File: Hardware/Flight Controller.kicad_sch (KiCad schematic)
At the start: 93 parts, among them J1 9V / 12V, J2 USB4110GFA, U1 TPS54302, U2 STM32F722RETx, U3 AP2112K-3.3, U4 TPS54302, U5 ICM-42688-P, U6 BMP388, U7 USBLC6-2SC6, U8 AT7456E, U9 INA226, Y1 27Mhz, Y2 8MHz

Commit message: this commit updates MCU shematics, Flash memory and Magnetometer
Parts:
- added C47, C49: 0.1uF, Capacitor_SMD:C_0603_1608Metric, symbol Device:C_Small
- added C48: 4.7uF, Capacitor_SMD:C_0603_1608Metric, symbol Device:C_Small
- added R27, R28: 4.7k, Resistor_SMD:R_0402_1005Metric, symbol Device:R_Small
- added R29, R30, R31: 10k, Resistor_SMD:R_0402_1005Metric, symbol Device:R_Small
- added U10: QMC5883P, easyeda2kicad:LGA-16_L3.0-W3.0-P0.50-BL_SQ, symbol Magneto:QMC5883P
- added U11: W25Q128JVSIQ, W25Q128JVSIQ:SOIC127P790X216-8N, symbol flash:W25Q128JVSIQ
- C25, C26: value 0.1uF -> 30pF
- C44: value 1uF -> 10nF
- C45, C46: value 0.1uF -> 14pF
- Y1: value 27Mhz -> 27Mhz 20pF
- Y2: value 8MHz -> 8MHz 12pF
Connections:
- net BARO_SCL is gone; now on net BMP_SCL: U2.28 (PB10)
- net +3.3V: now also C49.1, R27.1, R28.1, R29.2, R30.1, R31.2, U11.8 (VCC)
- net ADC_Voltage: now also U2.25 (PB0); no longer U2.61 (PB8)
- net BMP_SCL: no longer R11.2, U6.4 (SDI)
- net GND: now also U2.12 (VSSA), U2.18 (VSS), U2.31 (VSS), U2.47 (VSS), U2.63 (VSS), C47.2, C48.2, C49.2, U11.4 (GND)
- net OSD_CS: now also U2.33 (PB12)
- net OSD_MISO: now also U2.10 (PC2)
- net OSD_MOSI: now also U2.9 (PC1)
- net OSD_SCLK: now also U2.34 (PB13)
- net INA226_ALERT: now reaches U9.3 (~{Alert})
- net INA226_ALERT: now also U2.2 (PC13)
- net WIFI_TX: now reaches U2.14 (PA0)
- net WIFI_RX: now reaches U2.15 (PA1)
- net GPS_TX: now reaches U2.16 (PA2)
- net GPS_RX: now reaches U2.17 (PA3)
- net FLASH_MOSI: now reaches U2.27 (PB2)
- net FLASH_MOSI: now also U11.5 (DI(IO0))
- net SERVO_2: now reaches U2.35 (PB14)
- net SERVO_1: now reaches U2.36 (PB15)
- net TELEMETRY_TX: now reaches U2.37 (PC6)
- net TELEMETRY_RX: now reaches U2.38 (PC7)
- net FLASH_CS: now reaches U2.53 (PC12)
- net FLASH_CS: now also R29.1, U11.1 (/CS)
- net QMC_SDA: now reaches U2.62 (PB9)
- net QMC_SDA: now also R28.2, U10.16 (SDA)
- net BARO_SDA renamed BMP_SDA
- net BMP_SDA: now also R11.2, U6.4 (SDI)
- net Telemetry_RX renamed FLASH_MISO
- net FLASH_MISO: now also U11.2 (DO(IO1))
- net Telemetry_TX renamed FLASH_SCLK
- net FLASH_SCLK: now also U11.6 (CLK)
- new net: C48.1, U10.10 (C1), U10.11 (GND), U10.9 (GND)
- new net: C47.1, U10.2 (VDD)
- new net: R31.1, U11.3 (/WP(IO2))
- new net: R30.2, U11.7 (/HOLD/RESET(IO3))
- new net QMC_SCL: R27.2, U10.1 (SCK), U2.61 (PB8)
- no-connect marks 17 -> 27
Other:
- note added: "2*(12 - 5) = 14pF"
- note added: "2*(20-5) = 30pF"
- note added: "Flash Memory"
- note added: "Magnetometer"
- note added: "voltage sensor"
- moved on the sheet: C25, C26, C36, C37, C38, C39, C40, C41, C42, C43, C44, C45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

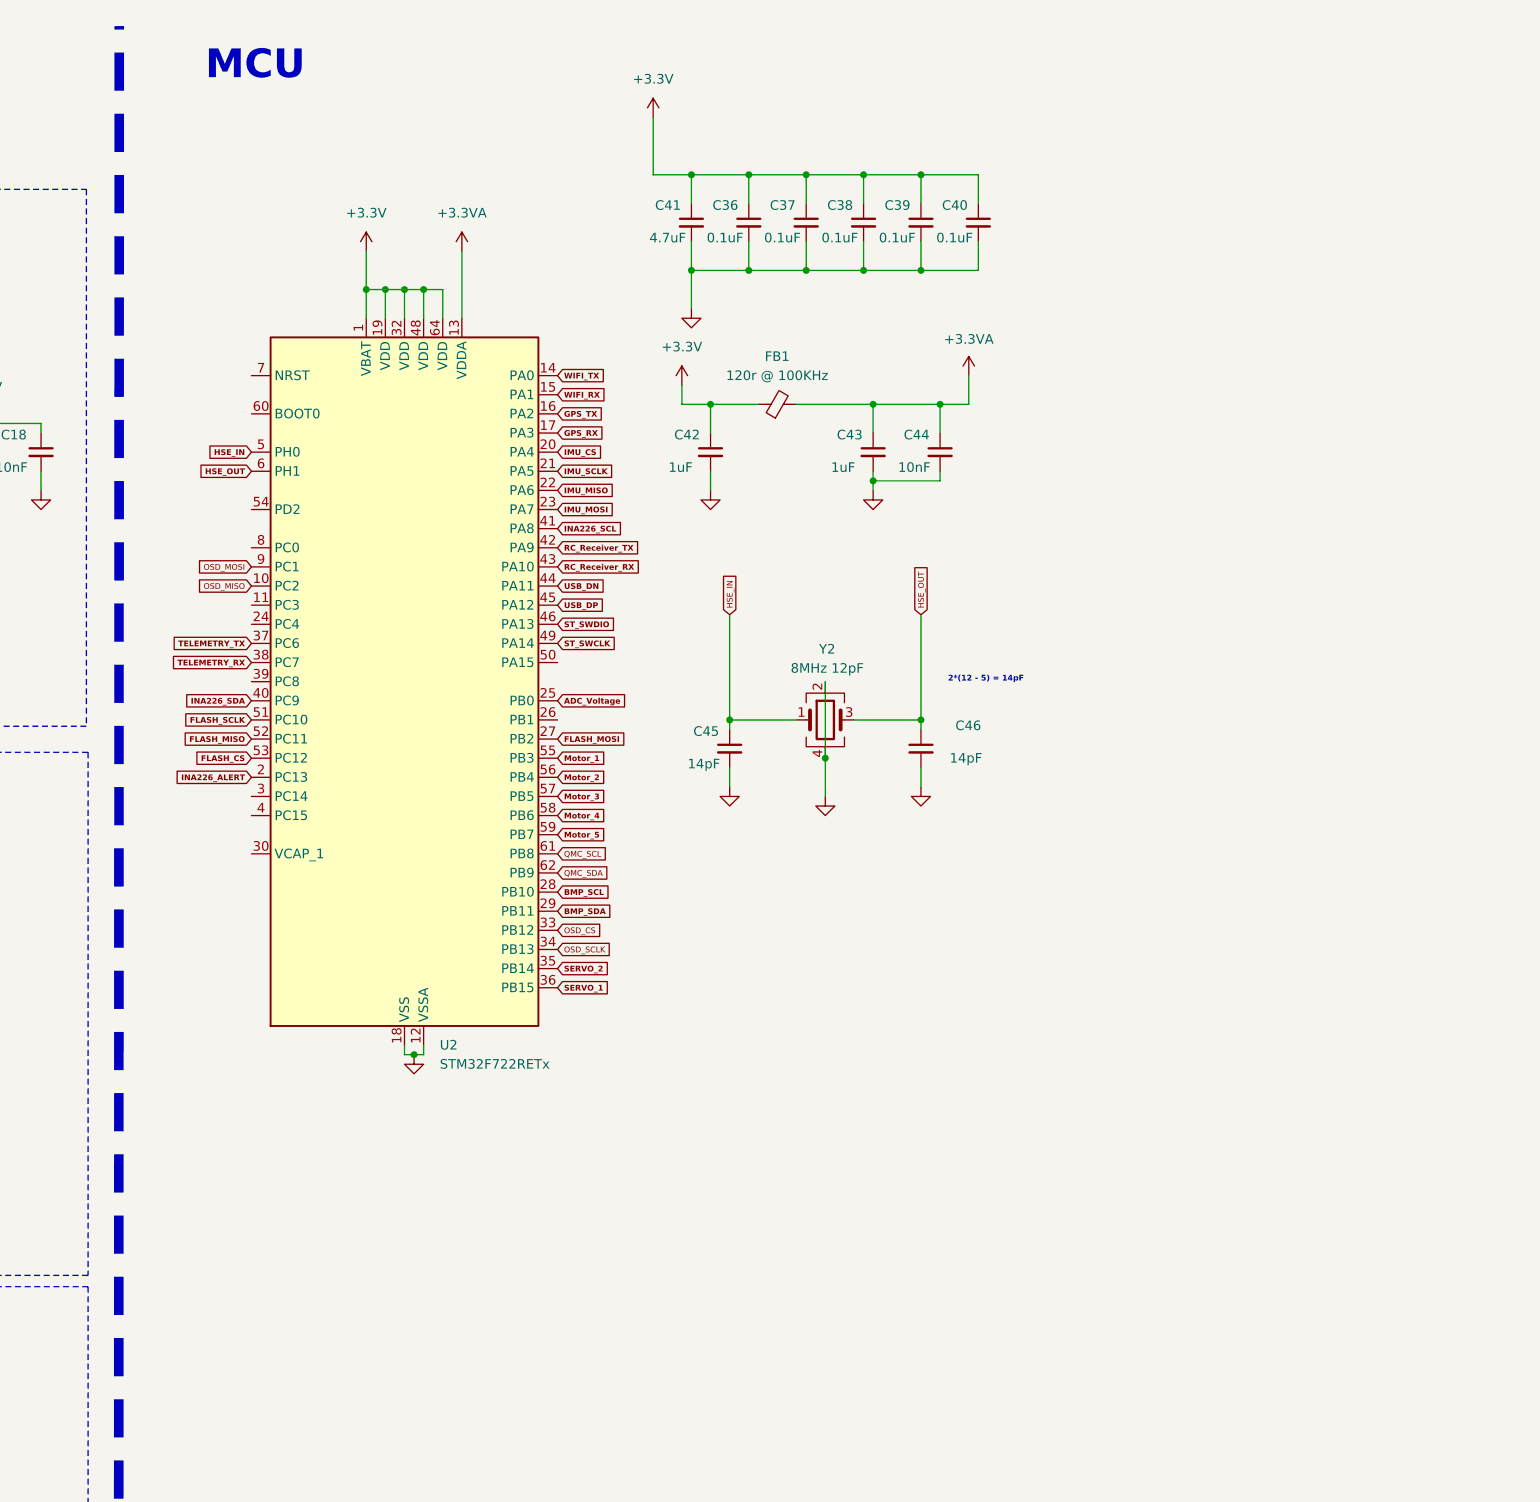
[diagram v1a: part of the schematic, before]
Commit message: This commit completes MCU and Crystals caps calculations
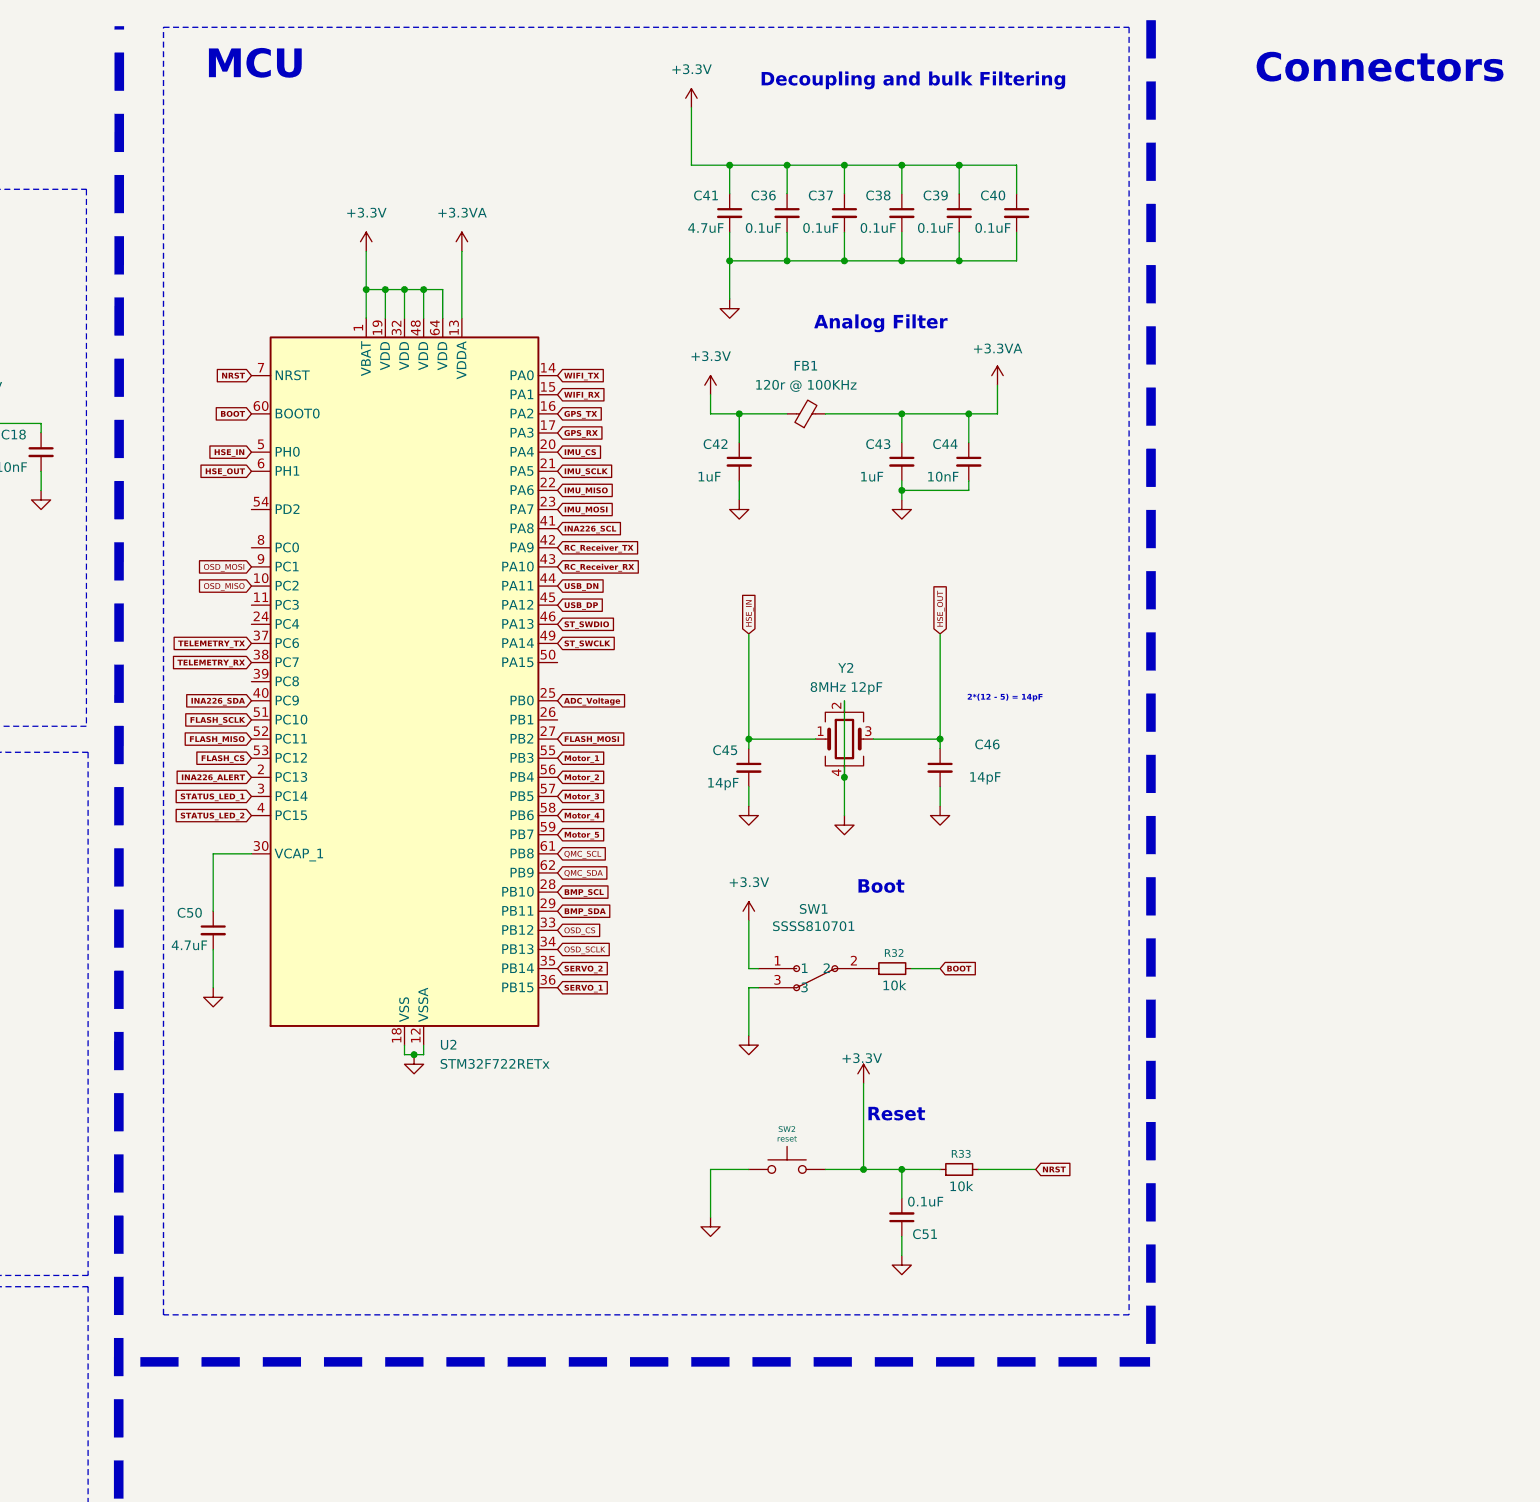
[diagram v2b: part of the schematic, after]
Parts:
- added C50: 4.7uF, Capacitor_SMD:C_0603_1608Metric, symbol Device:C_Small
- added C51: 0.1uF, Capacitor_SMD:C_0603_1608Metric, symbol Device:C_Small
- added R32, R33: 10k, Resistor_SMD:R_0402_1005Metric, symbol Device:R_Small
- added SW1: SSSS810701, easyeda2kicad:SW-SMD_SSSS810701, symbol switch-mine:SSSS810701
- added SW2: reset, Button_Switch_SMD:SW_Push_SPST_NO_Alps_SKRK, symbol Switch:SW_Push
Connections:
- net +3.3V: now also C51.2, R33.1, SW1.1, SW2.2
- net GND: now also C50.2, C51.1, SW1.3, SW2.1
- net STATUS_LED_1: now reaches U2.3 (PC14)
- net at U2.30 (VCAP_1): now also C50.1
- net STATUS_LED_2: now reaches U2.4 (PC15)
- net BOOT: now reaches U2.60 (BOOT0)
- net BOOT: now also R32.2
- net NRST: now reaches U2.7 (NRST)
- net NRST: now also R33.2
- new net: R32.1, SW1.2
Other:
- note added: "Analog Filter"
- note added: "Boot"
- note added: "Connectors"
- note added: "Decoupling and bulk Filtering"
- note added: "Reset"
- moved on the sheet: C36, C37, C38, C39, C40, C41, C42, C43, C44, C45, C46, FB1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

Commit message: This commit adds connectors in the schematics
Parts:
- removed D1: SS34, Diode_SMD:D_SMA, symbol Diode:SS34
- removed J1: 9V / 12V, Connector_PinHeader_2.54mm:PinHeader_1x03_P2.54mm_Vertical, symbol Connector_Generic:Conn_01x03
- added D2: PMEG3020EH, Diode_SMD:D_SOD-123F, symbol Diode:PMEG3020EH
- added J1: ST_LINK, Connector_PinHeader_2.54mm:PinHeader_1x04_P2.54mm_Horizontal, symbol Connector_Generic:Conn_01x04
- added JP1: 9V/12V, Jumper:SolderJumper-3_P1.3mm_Open_RoundedPad1.0x1.5mm_NumberLabels, symbol Jumper:SolderJumper_3_Open
- added R34: 0, Resistor_SMD:R_0402_1005Metric, symbol Device:R_Small
- added TP1, TP2, TP3, TP4: GPS, Solderpoint:Solderpad, symbol Connector:TestPoint
- added TP10: 9V/12V, Solderpoint:Solderpad, symbol Connector:TestPoint
- added TP11, TP12, TP13, TP14, TP9: GND, Solderpoint:Solderpad, symbol Connector:TestPoint
- added TP5, TP6: 3.3V, Solderpoint:Solderpad, symbol Connector:TestPoint
- added TP7, TP8: 5V, Solderpoint:Solderpad, symbol Connector:TestPoint
- FB1: footprint (none) -> Inductor_SMD:L_0603_1608Metric
- SW1: footprint easyeda2kicad:SW-SMD_SSSS810701 -> memo:SW-SMD_SSSS810701
- U10: footprint easyeda2kicad:LGA-16_L3.0-W3.0-P0.50-BL_SQ -> memo:QMC5883P
- U11: footprint W25Q128JVSIQ:SOIC127P790X216-8N -> memo:W25Q128JVSIQ
- Y1, Y2: footprint (none) -> Crystal:Crystal_SMD_3225-4Pin_3.2x2.5mm
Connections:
- net +3.3V: now also J1.1 (Pin_1), TP5.1, TP6.1
- net +5V: now also D2.1 (K), TP7.1, TP8.1
- net +5V_USB: now also D2.2 (A)
- net +pwr_out: now also TP10.1
- net BMP_INT: now also U2.11 (PC3)
- net BMP_SCL: no longer U2.28 (PB10), U6.2 (SCK)
- net BMP_SDA: no longer U2.29 (PB11), U6.4 (SDI)
- net GND: now also J1.4 (Pin_4), TP11.1, TP12.1, TP13.1, TP14.1, TP9.1
- net GPS_RX: now also TP2.1
- net GPS_TX: now also TP1.1
- net HSE_OUT: now also R34.2; no longer C46.1, Y2.3
- net IMU_INT1: now also U2.39 (PC8)
- net ST_SWCLK: now also J1.3 (Pin_3)
- net ST_SWDIO: now also J1.2 (Pin_2)
- net EN: now reaches R6.2, R7.1, U4.5 (EN)
- net FB: now reaches C14.2, R9.2, U4.4 (FB)
- net FB: now also JP1.2 (C)
- net FB_12V: now reaches R5C1.1
- net FB_12V: now also JP1.1 (A)
- net FB_9V: now reaches R5B1.1
- net FB_9V: now also JP1.3 (B)
- net FB_5V: now reaches C6.2, R4.2, R5.1, U1.4 (FB)
- net EN_5V: now reaches R1.2, R2.1, U1.5 (EN)
- net INA226_SCL renamed I2C2_SCL
- net I2C2_SCL: now also U2.28 (PB10), U6.2 (SCK); no longer U2.41 (PA8)
- net INA226_SDA renamed I2C2_SDA
- net I2C2_SDA: now also U2.29 (PB11), U6.4 (SDI); no longer U2.40 (PC9)
- new net: C46.1, R34.1, Y2.3
- new net GPS_SCL: TP4.1, U2.41 (PA8)
- new net GPS_SDA: TP3.1, U2.40 (PC9)
- no-connect marks 27 -> 32
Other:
- note added: "Debugger"
- note added: "GPS"
- note added: "Power"
- note added: "sharing same bus as BMP388"
- note added: "sharing same bus as INA226"
- moved on the sheet: R5B1, R5C1

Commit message: This commit changes the MCU and adds backup IMU
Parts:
- removed C50: 4.7uF, Capacitor_SMD:C_0603_1608Metric, symbol Device:C_Small
- removed U2: STM32F722RETx, Package_QFP:LQFP-64_10x10mm_P0.5mm, symbol MCU_ST_STM32F7:STM32F722RETx
- removed U3: AP2112K-3.3, Package_TO_SOT_SMD:SOT-23-5, symbol Regulator_Linear:AP2112K-3.3
- added C39, C44, C45: 0.1uF, Capacitor_SMD:C_0603_1608Metric, symbol Device:C_Small
- added C40, C41, C48: 2.2uF, Capacitor_SMD:C_0603_1608Metric, symbol Device:C_Small
- added C52: 10nF, Capacitor_SMD:C_0603_1608Metric, symbol Device:C_Small
- added J3: RC Receiver, Connector_JST:JST_GH_SM04B-GHS-TB_1x04-1MP_P1.25mm_Horizontal, symbol Connector_Generic:Conn_01x04
- added R12, R19, R34: 0, Resistor_SMD:R_0402_1005Metric, symbol Device:R_Small
- added TP12, TP17, TP20, TP6, TP7: GND, Solderpoint:Solderpad, symbol Connector:TestPoint
- added TP14: Motor_3, Solderpoint:Solderpad, symbol Connector:TestPoint
- added TP19: Motor_4, Solderpoint:Solderpad, symbol Connector:TestPoint
- added TP2: Motor 1, Solderpoint:Solderpad, symbol Connector:TestPoint
- added TP3: Motor_5, Solderpoint:Solderpad, symbol Connector:TestPoint
- added TP9: Motor 2, Solderpoint:Solderpad, symbol Connector:TestPoint
- added U11: STM32H743VITx, Package_QFP:LQFP-100_14x14mm_P0.5mm, symbol MCU_ST_STM32H7:STM32H743VITx
- added U12: ICM-42688-P, memo:PQFN50P300X250X97-14N, symbol ICM-42688:ICM-42688-P
- added U3: AZ1117-3.3, Package_TO_SOT_SMD:SOT-223, symbol Regulator_Linear:AZ1117-3.3
- C12: renamed from C8; value 0.1uF -> 22uF
- C6: renamed from C7; value 0.1uF -> 10uF
- renumbered C9 to C1, C12 to C10, C4 to C11, C5 to C14, C14 to C15, C6 to C16, C31 to C17, C27 to C18, C32 to C19, C1 to C2, C25 to C20, C33 to C21, C26 to C24, C28 to C25, C35 to C26, C30 to C27, C24 to C28, C10 to C3, C34 to C30, C47 to C31, C19 to C32, C48 to C33, C16 to C34, C20 to C35, C17 to C36, C49 to C37, C18 to C38, C2 to C4, C41 to C42, C42 to C43, C45 to C46, C36 to C47, C37 to C49, C15 to C5, C51 to C50, C43 to C51, C38 to C53, C44 to C54, C46 to C55, C39 to C56, C40 to C57, C21 to C7, C11 to C8, C3 to C9, D2 to D1, D3 to D2, J2 to J1, J1 to J2, L3 to L1, L1 to L3, R13 to R1, R4 to R10, R5 to R11, R17 to R13, R18 to R14, R21 to R15, R22 to R16, R23 to R17, R24 to R18, R14 to R2, R15 to R20, R25 to R21, R26 to R22, R16 to R23, R20 to R24, R19 to R25, R12 to R26, R10 to R27, R11 to R28, R27 to R29, R6 to R3, R28 to R30, R30 to R32, R29 to R33, R32 to R35, R33 to R36, R34 to R37, R7 to R4, R1 to R5, R2 to R6, R8 to R7, R9 to R8, R3 to R9, SW2 to SW1, SW1 to SW2, TP9 to TP1, TP6 to TP10, TP8 to TP11, TP12 to TP13, TP13 to TP15, TP10 to TP16, TP14 to TP18, TP1 to TP21, TP2 to TP22, TP3 to TP23, TP4 to TP24, TP5 to TP4, TP7 to TP5, TP11 to TP8, U4 to U1, U11 to U10, U1 to U2, U7 to U4, U9 to U5, U8 to U6, U5 to U7, U10 to U8, U6 to U9
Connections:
- net +3.3V: now also C44.1, C45.1, C48.1, C52.1, U11.100 (VDD), U11.11 (VDD), U11.27 (VDD), U11.50 (VDD), U11.6 (VBAT), U11.75 (VDD), U12.5 (VDDIO), U12.8 (VDD), U3.2 (VO)
- net +3.3VA: now also C39.1, U11.20 (VREF+), U11.21 (VDDA)
- net +5V: now also J3.1 (Pin_1), R19.1, R19.2, U3.3 (VI)
- net ADC_VOLTAGE: now also U11.17 (PC2_C)
- net BMP_INT: now also U11.51 (PB12)
- net BOOT: now also U11.94 (BOOT0)
- net FLASH_CS: now also U11.88 (PD7)
- net FLASH_MISO: now also U11.90 (PB4)
- net FLASH_MOSI: now also U11.91 (PB5)
- net FLASH_SCLK: now also U11.89 (PB3)
- net GND: now also C39.2, C40.1, C41.1, C44.2, C45.2, C48.2, C52.2, J3.4 (Pin_4), R34.1, TP12.1, TP17.1, TP20.1, TP6.1, TP7.1, U11.10 (VSS), U11.19 (VSSA), U11.26 (VSS), U11.49 (VSS), U11.74 (VSS), U11.99 (VSS), U12.11 (RESV_11), U12.6 (GND), U12.7 (RESV_7), U3.1 (GND)
- net GPS_RX: now also U11.25 (PA3)
- net GPS_SCL: now also U11.67 (PA8)
- net GPS_SDA: now also U11.66 (PC9)
- net GPS_TX: now also U11.24 (PA2)
- net HSE_IN: now also U11.12 (PH0)
- net HSE_OUT: now also U11.13 (PH1)
- net I2C2_SCL: now also U11.46 (PB10)
- net I2C2_SDA: now also U11.47 (PB11)
- net IMU_CS: now also U11.28 (PA4)
- net IMU_INT1: now also U11.32 (PC4)
- net IMU_MISO: now also U11.30 (PA6)
- net IMU_MOSI: now also U11.31 (PA7)
- net IMU_SCLK: now also U11.29 (PA5)
- net INA226_ALERT: now also U11.15 (PC0)
- net Motor_1: now also TP2.1, U11.62 (PD15)
- net Motor_2: now also TP9.1, U11.61 (PD14)
- net Motor_3: now also TP14.1, U11.60 (PD13)
- net Motor_4: now also TP19.1, U11.59 (PD12)
- net Motor_5: now also TP3.1
- net NRST: now also U11.14 (NRST)
- net OSD_CS: now also U11.2 (PE3)
- net OSD_MISO: now also U11.4 (PE5)
- net OSD_MOSI: now also U11.5 (PE6)
- net OSD_SCLK: now also U11.1 (PE2)
- net QMC_SCL: now also U11.95 (PB8)
- net QMC_SDA: now also U11.96 (PB9)
- net SERVO_1: now also U11.64 (PC7)
- net SERVO_2: now also U11.65 (PC8)
- net STATUS_LED_1: now also U11.34 (PB0)
- net STATUS_LED_2: now also U11.33 (PC5)
- net ST_SWCLK: now also U11.76 (PA14)
- net ST_SWDIO: now also U11.72 (PA13)
- net TELEMETRY_RX: now also U11.56 (PD9)
- net TELEMETRY_TX: now also U11.55 (PD8)
- net USB_DN: now also U11.70 (PA11)
- net USB_DP: now also U11.71 (PA12)
- net VBAT_Filtered: now also R12.1; no longer C17.1, C19.1, C21.1, R24.4, U5.8 (Vbus)
- new net: C41.2, U11.73 (VCAP)
- new net: R34.2, U12.9 (INT2/FSYNC/CLKIN)
- new net: C40.2, U11.48 (VCAP)
- new net IMU2_CS: U11.81 (PD0), U12.12 (AP_CS)
- new net IMU2_INT1: U11.82 (PD1), U12.4 (INT1/INT)
- new net IMU2_MISO: U11.79 (PC11), U12.1 (AP_SDO/AP_AD0)
- new net IMU2_MOSI: U11.80 (PC12), U12.14 (AP_SDA/AP_SDIO/AP_SDI)
- new net IMU2_SCLK: U11.78 (PC10), U12.13 (AP_SCL/AP_SCLK)
- new net LED_STRIPS: U11.35 (PB1)
- new net SERVO_3: U11.22 (PA0)
- new net T1_CH1: U11.39 (PE9)
- new net T1_CH2: U11.41 (PE11)
- new net T1_CH3: U11.43 (PE13)
- new net T1_CH4: U11.44 (PE14)
- new net T2_CH1: U11.77 (PA15)
- new net VBAT_Sense: C17.1, C19.1, C21.1, R12.2, R24.4, U5.8 (Vbus)
- new net WIFI/RC_RX: J3.3 (Pin_3), U11.54 (PB15)
- new net WIFI/RC_TX: J3.2 (Pin_2), U11.53 (PB14)
- no-connect marks 32 -> 58
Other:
- note added: "Backup IMU"
- note added: "Motors PWM pins"
- moved on the sheet: C42, C43, C46, C47, C49, C50, C51, C53, C54, C55, C56, C57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
